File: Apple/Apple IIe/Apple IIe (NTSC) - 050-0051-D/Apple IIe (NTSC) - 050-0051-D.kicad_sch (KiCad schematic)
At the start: 0 parts

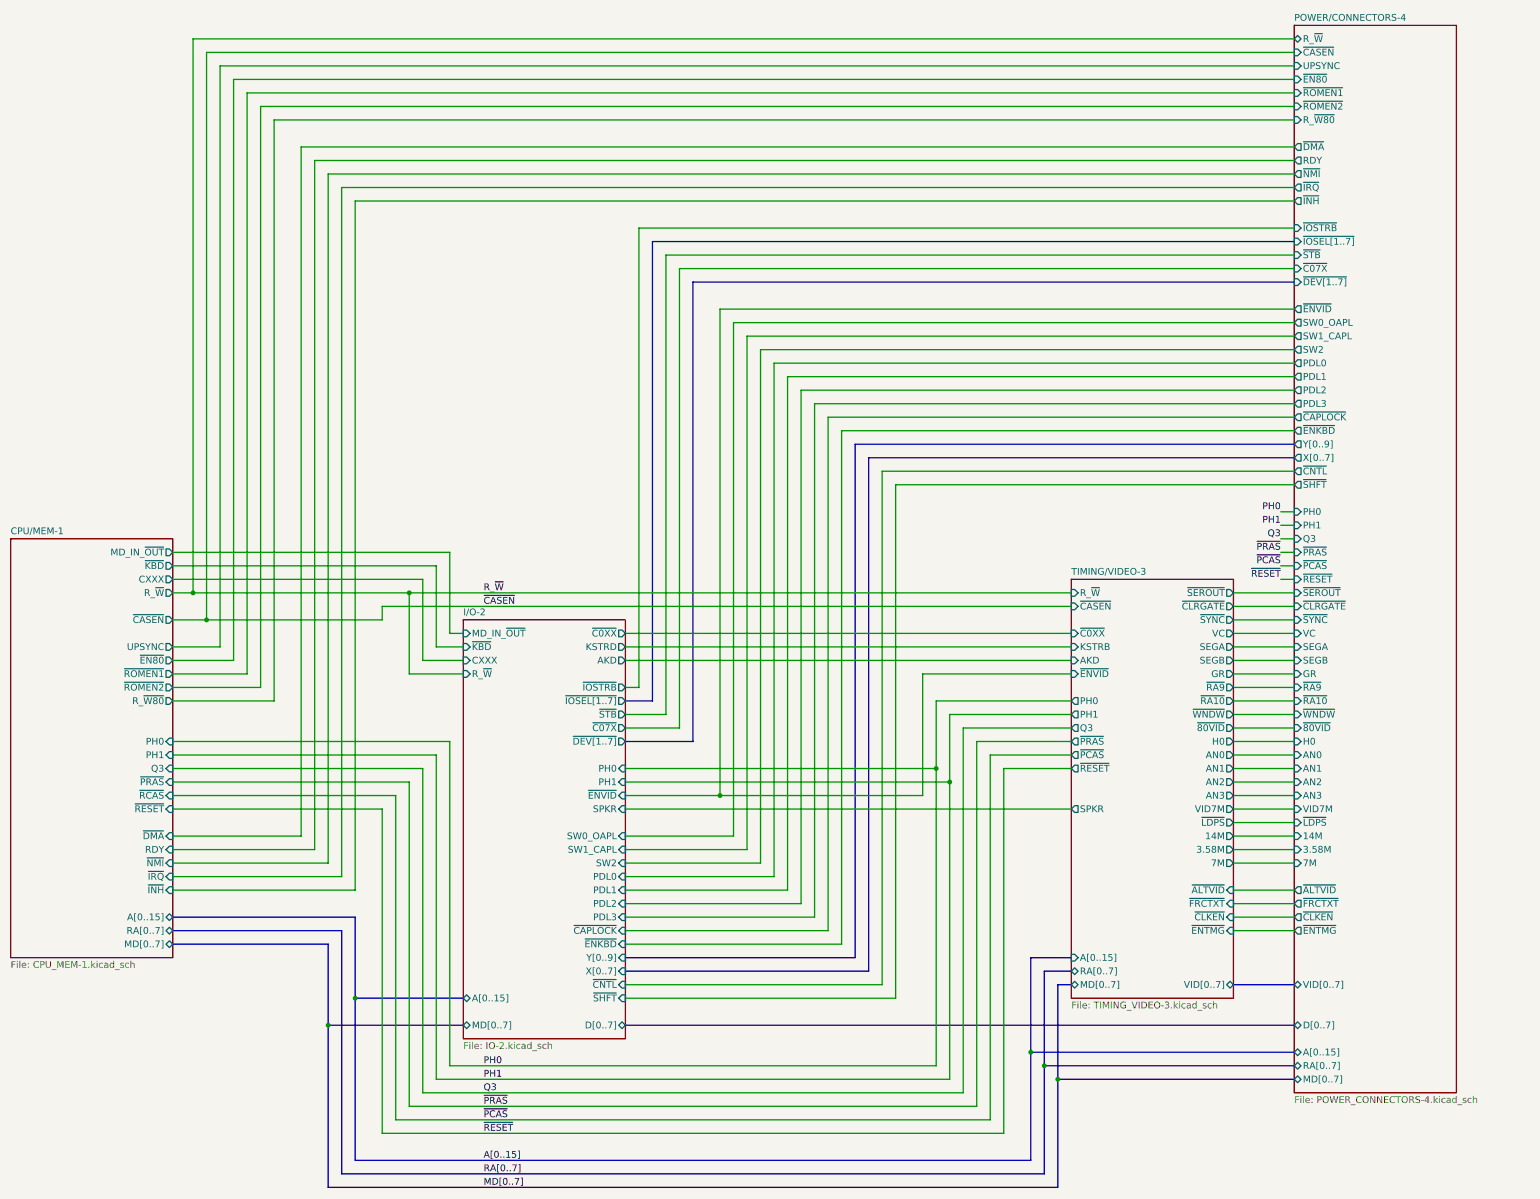
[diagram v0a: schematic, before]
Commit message: update IIe library to v7
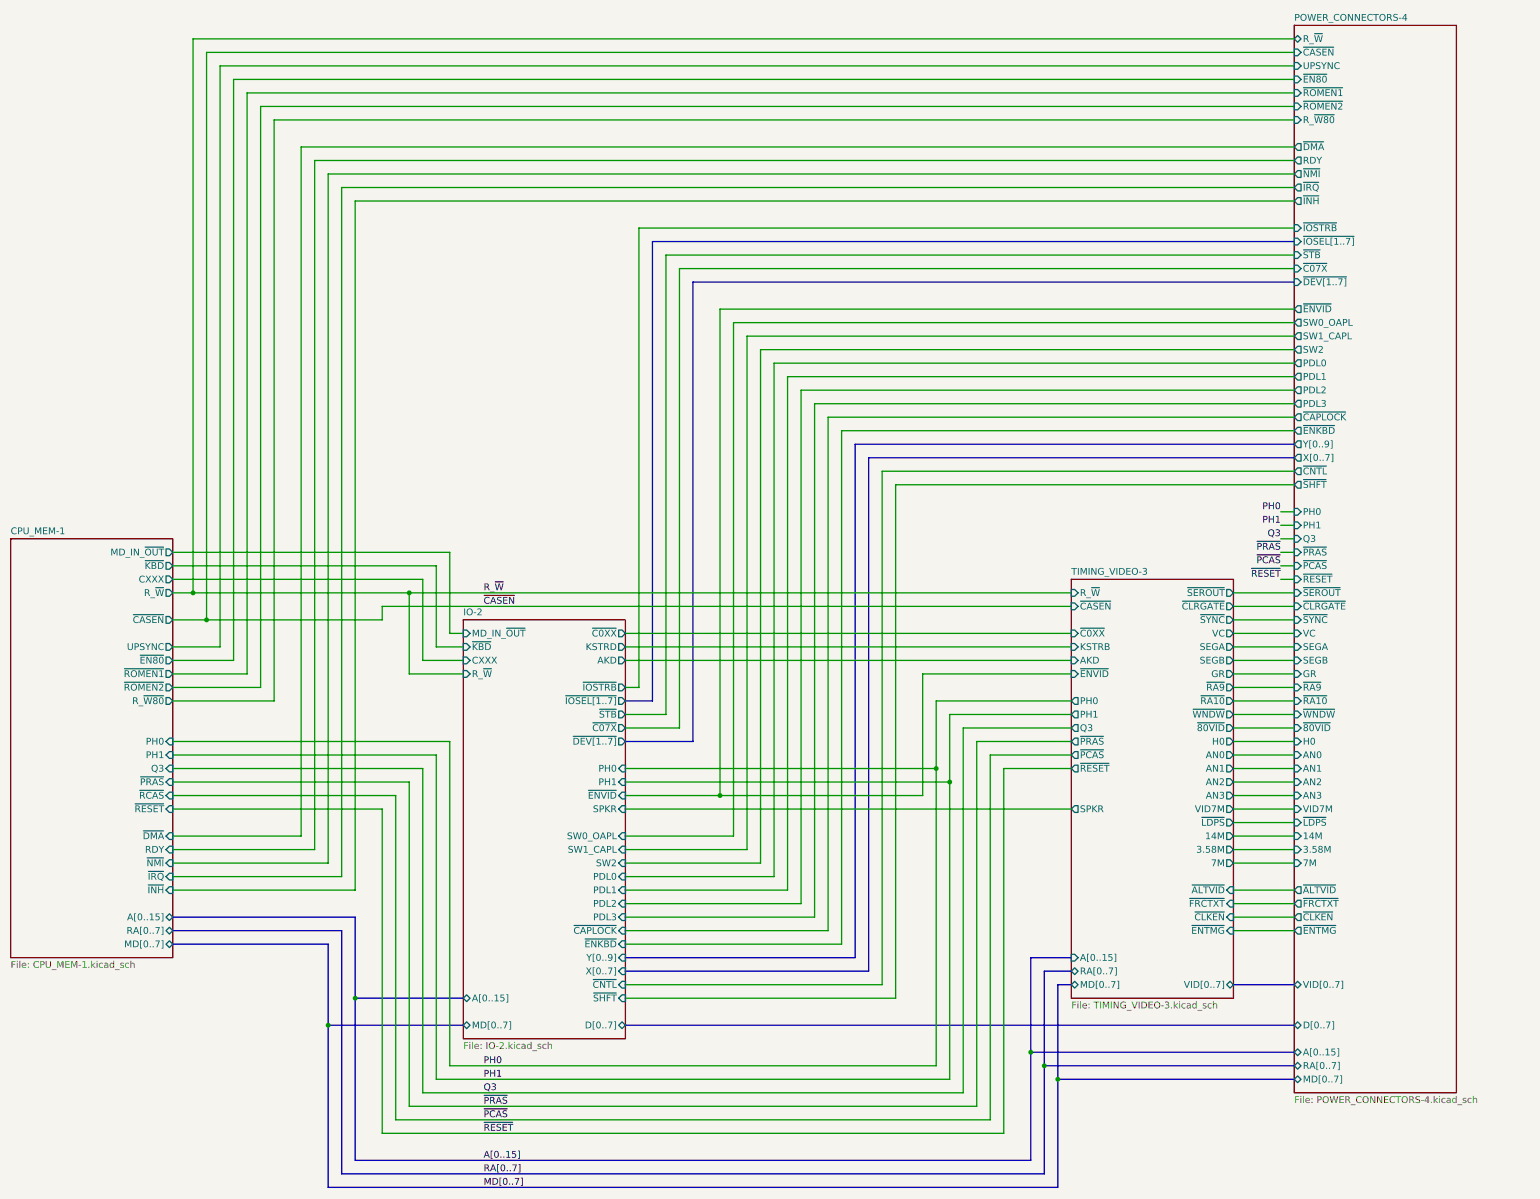
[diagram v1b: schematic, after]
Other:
- sheet CPU/MEM-1 renamed CPU_MEM-1
- sheet I/O-2 renamed IO-2
- sheet POWER/CONNECTORS-4 renamed POWER_CONNECTORS-4
- sheet TIMING/VIDEO-3 renamed TIMING_VIDEO-3
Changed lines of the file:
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@@
   (title_block
     (title "Apple IIe Computer (NTSC) 050-0051-D")
+    (rev "2")
   )
   (junction (at 100.33 148.59) (diameter 0) (color 0 0 0 0)
@@
   (sheet (at 63.5 133.35) (size 30.48 78.74) (fields_autoplaced)
     (stroke (width 0) (type solid))
-    (fill (color 0 0 0 0.0000))
-    (property "Sheetname" "CPU/MEM-1" (at 63.5 132.6384 0)
+    (fill (color 255 255 255 1.0000))
+    (property "Sheetname" "CPU_MEM-1" (at 63.5 132.6384 0)
       (effects (font (size 1.27 1.27)) (justify left bottom))
     )
@@
   (sheet (at 148.59 148.59) (size 30.48 78.74) (fields_autoplaced)
     (stroke (width 0) (type solid))
-    (fill (color 0 0 0 0.0000))
-    (property "Sheetname" "I/O-2" (at 148.59 147.8784 0)
+    (fill (color 255 255 255 1.0000))
+    (property "Sheetname" "IO-2" (at 148.59 147.8784 0)
       (effects (font (size 1.27 1.27)) (justify left bottom))
     )
@@
   (sheet (at 262.89 140.97) (size 30.48 78.74) (fields_autoplaced)
     (stroke (width 0) (type solid))
-    (fill (color 0 0 0 0.0000))
-    (property "Sheetname" "TIMING/VIDEO-3" (at 262.89 140.2584 0)
+    (fill (color 255 255 255 1.0000))
+    (property "Sheetname" "TIMING_VIDEO-3" (at 262.89 140.2584 0)
       (effects (font (size 1.27 1.27)) (justify left bottom))
     )
@@
   (sheet (at 304.8 36.83) (size 30.48 200.66) (fields_autoplaced)
     (stroke (width 0) (type solid))
-    (fill (color 0 0 0 0.0000))
-    (property "Sheetname" "POWER/CONNECTORS-4" (at 304.8 36.1184 0)
+    (fill (color 255 255 255 1.0000))
+    (property "Sheetname" "POWER_CONNECTORS-4" (at 304.8 36.1184 0)
       (effects (font (size 1.27 1.27)) (justify left bottom))
     )
